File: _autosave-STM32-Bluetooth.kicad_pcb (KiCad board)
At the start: 4 copper layers, 41 parts, among them J1 USB_C_Receptacle_USB2.0_16P, J2 TC2030, J3 Conn_01x04, J4 Conn_Coaxial, SW1 SW_Push, U2 STM32WB55CEU6, U3 MIC5365-3.3YD5, X1 32kHz768, X2 32MHz

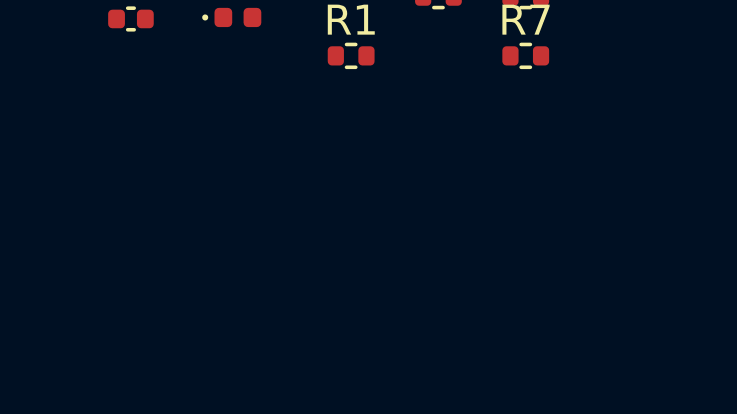
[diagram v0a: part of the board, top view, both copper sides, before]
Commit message: Added footprints and PCB editor
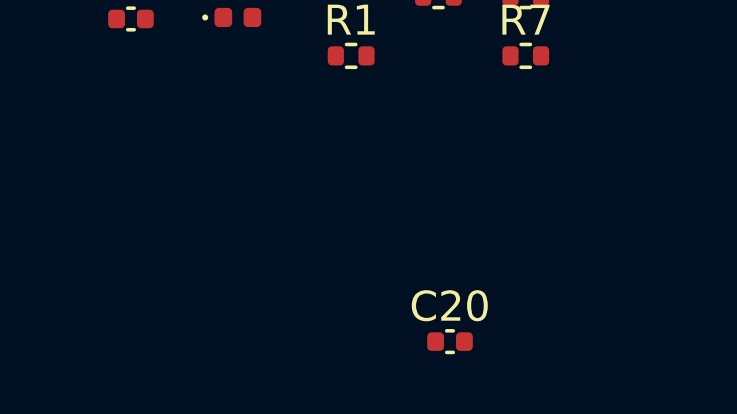
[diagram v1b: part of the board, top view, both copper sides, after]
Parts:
- added C20: 0p8, Capacitor_SMD:C_0402_1005Metric, F.Cu at (139.5, 110.5)
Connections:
- J2 pad 3: /SWD_NRST -> unconnected-(J2-~{RESET}-Pad3)
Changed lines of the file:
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@@
 	(net 51 "unconnected-(U2-PA4-Pad13)")
 	(net 52 "unconnected-(U3-NC-Pad4)")
+	(net 53 "unconnected-(J2-~{RESET}-Pad3)")
 	(footprint "Capacitor_SMD:C_0402_1005Metric"
 		(layer "F.Cu")
@@
 		)
 	)
+	(footprint "Capacitor_SMD:C_0402_1005Metric"
+		(layer "F.Cu")
+		(at 139.5 110.5)
+		(descr "Capacitor SMD 0402 (1005 Metric), square (rectangular) end terminal, IPC-7351 nominal, (Body size source: IPC-SM-782 page 76, https://www.pcb-3d.com/wordpress/wp-content/uploads/ipc-sm-782a_amendment_1_and_2.pdf), generated with kicad-footprint-generator")
+		(tags "capacitor")
+		(property "Reference" "C20"
+			(at 0 -1.16 0)
+			(layer "F.SilkS")
+			(effects
+				(font
+					(size 1 1)
+					(thickness 0.15)
+				)
+			)
+		)
+		(property "Value" "0p8"
+			(at 0 1.16 0)
+			(layer "F.Fab")
+			(effects
+				(font
+					(size 1 1)
+					(thickness 0.15)
+				)
+			)
+		)
+		(property "Datasheet" ""
+			(at 0 0 0)
+			(layer "F.Fab")
+			(hide yes)
+			(effects
+				(font
+					(size 1.27 1.27)
+					(thickness 0.15)
+				)
+			)
+		)
+		(property "Description" "Unpolarized capacitor"
+			(at 0 0 0)
+			(layer "F.Fab")
+			(hide yes)
+			(effects
+				(font
+					(size 1.27 1.27)
+					(thickness 0.15)
+				)
+			)
+		)
+		(property "Distributor Link" ""
+			(at 0 0 0)
+			(unlocked yes)
+			(layer "F.Fab")
+			(hide yes)
+			(effects
+				(font
+					(size 1 1)
+					(thickness 0.15)
+				)
+			)
+		)
+		(property "Manufacturer" ""
+			(at 0 0 0)
+			(unlocked yes)
+			(layer "F.Fab")
+			(hide yes)
+			(effects
+				(font
+					(size 1 1)
+					(thickness 0.15)
+				)
+			)
+		)
+		(property "Manufacturer Part Number" ""
+			(at 0 0 0)
+			(unlocked yes)
+			(layer "F.Fab")
+			(hide yes)
+			(effects
+				(font
+					(size 1 1)
+					(thickness 0.15)
+				)
+			)
+		)
+		(property ki_fp_filters "C_*")
+		(sheetname "/")
+		(sheetfile "STM32-Bluetooth.kicad_sch")
+		(attr smd)
+		(fp_line
+			(start -0.107836 -0.36)
+			(end 0.107836 -0.36)
+			(stroke
+				(width 0.12)
+				(type solid)
+			)
+			(layer "F.SilkS")
+		)
+		(fp_line
+			(start -0.107836 0.36)
+			(end 0.107836 0.36)
+			(stroke
+				(width 0.12)
+				(type solid)
+			)
+			(layer "F.SilkS")
+		)
+		(fp_line
+			(start -0.91 -0.46)
+			(end 0.91 -0.46)
+			(stroke
+				(width 0.05)
+				(type solid)
+			)
+			(layer "F.CrtYd")
+		)
+		(fp_line
+			(start -0.91 0.46)
+			(end -0.91 -0.46)
+			(stroke
+				(width 0.05)
+				(type solid)
+			)
+			(layer "F.CrtYd")
+		)
+		(fp_line
+			(start 0.91 -0.46)
+			(end 0.91 0.46)
+			(stroke
+				(width 0.05)
+				(type solid)
+			)
+			(layer "F.CrtYd")
+		)
+		(fp_line
+			(start 0.91 0.46)
+			(end -0.91 0.46)
+			(stroke
+				(width 0.05)
+				(type solid)
+			)
+			(layer "F.CrtYd")
+		)
+		(fp_line
+			(start -0.5 -0.25)
+			(end 0.5 -0.25)
+			(stroke
+				(width 0.1)
+				(type solid)
+			)
+			(layer "F.Fab")
+		)
+		(fp_line
+			(start -0.5 0.25)
+			(end -0.5 -0.25)
+			(stroke
+				(width 0.1)
+				(type solid)
+			)
+			(layer "F.Fab")
+		)
+		(fp_line
+			(start 0.5 -0.25)
+			(end 0.5 0.25)
+			(stroke
+				(width 0.1)
+				(type solid)
+			)
+			(layer "F.Fab")
+		)
+		(fp_line
+			(start 0.5 0.25)
+			(end -0.5 0.25)
+			(stroke
+				(width 0.1)
+				(type solid)
+			)
+			(layer "F.Fab")
+		)
+		(fp_text user "${REFERENCE}"
+			(at 0 0 0)
+			(layer "F.Fab")
+			(effects
+				(font
+					(size 0.25 0.25)
+					(thickness 0.04)
+				)
+			)
+		)
+		(pad "1" smd roundrect
+			(at -0.48 0)
+			(size 0.56 0.62)
+			(layers "F.Cu" "F.Mask" "F.Paste")
+			(roundrect_rratio 0.25)
+			(net 7 "Net-(U2-RF1)")
+			(pintype "passive")
+		)
+		(pad "2" smd roundrect
+			(at 0.48 0)
+			(size 0.56 0.62)
+			(layers "F.Cu" "F.Mask" "F.Paste")
+			(roundrect_rratio 0.25)
+			(net 1 "+3V3")
+			(pintype "passive")
+		)
+		(embedded_fonts no)
+		(model "${KICAD9_3DMODEL_DIR}/Capacitor_SMD.3dshapes/C_0402_1005Metric.wrl"
+			(offset
+				(xyz 0 0 0)
+			)
+			(scale
+				(xyz 1 1 1)
+			)
+			(rotate
+				(xyz 0 0 0)
+			)
+		)
+	)
 	(footprint "Capacitor_SMD:C_0603_1608Metric"
 		(layer "F.Cu")
@@
 			(size 0.7874 0.7874)
 			(layers "F.Cu" "F.Mask")
-			(net 5 "/SWD_NRST")
+			(net 53 "unconnected-(J2-~{RESET}-Pad3)")
 			(pinfunction "~{RESET}")
 			(pintype "open_collector")
